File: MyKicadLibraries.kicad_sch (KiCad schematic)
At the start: 38 parts, among them J1 Conn_01x08, J10 RCJ-22, J11 DIN-5, J12 Mini-DIN-6, J13 USB_A, J14 Conn_01x02, J15 Conn_01x02, J2 Conn_01x08, J3 POGO Pins, J4 c8-inlet, J5 FTDI, J6 Micro_SD_Card, J7 Conn_01x04, J8 Conn_02x04_Counter_Clockwise, J9 Conn_01x04, SW1 Schurter Switch, U1 radio-receiver, U10 rdm-6300, U11 magnetic-charger, U12 adafruit-MAX98357, U13 TTL, U14 lxb18, U15 esp32-wemos-d1-mini, U16 TCRT5000, U17 opb607a, U18 max98367, U19 esp-01f, U2 TP4056, U3 LilygoSIMT7000G, U4 esp-01m, U5 relais_module, U6 ESP-01, U7 dcdc, U8 mems-mic, U9 ESP-12E

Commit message: Update tp4056 and fix edge cut issues
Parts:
- removed BT1: Battery_Cell, symbol Device:Battery_Cell
- removed U2: TP4056, TP4056:TP4056, symbol TP4056:TP4056
- added U2: tp4056, tp4056:tp4056, symbol TP4056:tp4056
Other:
- moved on the sheet: J6, U15, U19
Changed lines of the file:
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@@
     (pin "1")
-  )
-  (symbol (lib_id "Device:Battery_Cell") (at 121.92 158.75 0) (unit 1)
-    (in_bom yes) (on_board yes)
-    (property "Reference" "BT1" (id 0) (at 115.824 161.798 90)
-      (effects (font (size 1.27 1.27)) (justify left))
-    )
-    (property "Value" "Battery_Cell" (id 1) (at 118.364 161.798 90)
-      (effects (font (size 1.27 1.27)) (justify left))
-    )
-    (property "Footprint" "" (id 2) (at 121.92 157.226 90)
-      (effects (font (size 1.27 1.27)) hide)
-    )
-    (property "Datasheet" "~" (id 3) (at 121.92 157.226 90)
-      (effects (font (size 1.27 1.27)) hide)
-    )
-    (pin "1")
-    (pin "2")
   )
   (symbol (lib_id "Connector:DIN-5") (at 158.75 97.79 0) (unit 1)
@@
     (pin "9")
   )
-  (symbol (lib_id "esp32-wemos-d1-mini:esp32-wemos-d1-mini") (at -22.098 87.376 0) (unit 1)
-    (in_bom yes) (on_board yes) (fields_autoplaced)
-    (property "Reference" "U15" (id 0) (at -21.463 83.82 0))
-    (property "Value" "esp32-wemos-d1-mini" (id 1) (at -21.463 86.36 0))
-    (property "Footprint" "esp32-wemos-d1-mini:esp32-wemos-d1-mini" (id 2) (at -18.288 84.836 0)
-      (effects (font (size 1.27 1.27)) hide)
-    )
-    (property "Datasheet" "" (id 3) (at -18.288 84.836 0)
+  (symbol (lib_id "esp32-wemos-d1-mini:esp32-wemos-d1-mini") (at 276.86 38.1 0) (unit 1)
+    (in_bom yes) (on_board yes) (fields_autoplaced)
+    (property "Reference" "U15" (id 0) (at 277.495 34.544 0))
+    (property "Value" "esp32-wemos-d1-mini" (id 1) (at 277.495 37.084 0))
+    (property "Footprint" "esp32-wemos-d1-mini:esp32-wemos-d1-mini" (id 2) (at 280.67 35.56 0)
+      (effects (font (size 1.27 1.27)) hide)
+    )
+    (property "Datasheet" "" (id 3) (at 280.67 35.56 0)
       (effects (font (size 1.27 1.27)) hide)
     )
@@
     (pin "8")
   )
-  (symbol (lib_id "TP4056:TP4056") (at 129.54 157.48 0) (unit 1)
-    (in_bom yes) (on_board yes) (fields_autoplaced)
-    (property "Reference" "U2" (id 0) (at 131.5594 146.05 0)
-      (effects (font (size 1.27 1.27)) (justify left))
-    )
-    (property "Value" "TP4056" (id 1) (at 131.5594 148.59 0)
-      (effects (font (size 1.27 1.27)) (justify left))
-    )
-    (property "Footprint" "TP4056:TP4056" (id 2) (at 128.27 131.445 0)
-      (effects (font (size 1.27 1.27)) hide)
-    )
-    (property "Datasheet" "" (id 3) (at 128.27 131.445 0)
-      (effects (font (size 1.27 1.27)) hide)
-    )
-    (pin "1")
-    (pin "2")
-    (pin "3")
-    (pin "4")
-    (pin "5")
-    (pin "6")
-  )
-  (symbol (lib_id "Connector:Micro_SD_Card") (at 83.566 172.466 0) (unit 1)
-    (in_bom yes) (on_board yes) (fields_autoplaced)
-    (property "Reference" "J6" (id 0) (at 84.201 152.654 0))
-    (property "Value" "Micro_SD_Card" (id 1) (at 84.201 155.194 0))
-    (property "Footprint" "sd-card:sd-card" (id 2) (at 112.776 164.846 0)
-      (effects (font (size 1.27 1.27)) hide)
-    )
-    (property "Datasheet" "http://katalog.we-online.de/em/datasheet/693072010801.pdf" (id 3) (at 83.566 172.466 0)
+  (symbol (lib_id "Connector:Micro_SD_Card") (at 39.37 176.53 0) (unit 1)
+    (in_bom yes) (on_board yes) (fields_autoplaced)
+    (property "Reference" "J6" (id 0) (at 40.005 156.718 0))
+    (property "Value" "Micro_SD_Card" (id 1) (at 40.005 159.258 0))
+    (property "Footprint" "sd-card:sd-card" (id 2) (at 68.58 168.91 0)
+      (effects (font (size 1.27 1.27)) hide)
+    )
+    (property "Datasheet" "http://katalog.we-online.de/em/datasheet/693072010801.pdf" (id 3) (at 39.37 176.53 0)
       (effects (font (size 1.27 1.27)) hide)
     )
@@
     (pin "3")
   )
-  (symbol (lib_id "esp-01F:esp-01f") (at -73.787 111.125 0) (unit 1)
-    (in_bom yes) (on_board yes) (fields_autoplaced)
-    (property "Reference" "U19" (id 0) (at -73.787 85.09 0))
-    (property "Value" "esp-01f" (id 1) (at -73.787 87.63 0))
-    (property "Footprint" "esp-01f:esp-01f" (id 2) (at -87.122 142.875 0)
+  (symbol (lib_id "esp-01F:esp-01f") (at 86.36 167.64 0) (unit 1)
+    (in_bom yes) (on_board yes) (fields_autoplaced)
+    (property "Reference" "U19" (id 0) (at 86.36 141.605 0))
+    (property "Value" "esp-01f" (id 1) (at 86.36 144.145 0))
+    (property "Footprint" "esp-01f:esp-01f" (id 2) (at 73.025 199.39 0)
       (effects (font (size 1.27 1.27)) (justify bottom) hide)
     )
-    (property "Datasheet" "http://www.ai-thinker.com/pro_view-62.html" (id 3) (at -72.517 139.7 0)
+    (property "Datasheet" "http://www.ai-thinker.com/pro_view-62.html" (id 3) (at 87.63 196.215 0)
       (effects (font (size 1.27 1.27)) hide)
     )
@@
     (pin "4")
   )
+  (symbol (lib_id "TP4056:tp4056") (at 26.67 73.66 0) (unit 1)
+    (in_bom yes) (on_board yes) (fields_autoplaced)
+    (property "Reference" "U2" (id 0) (at 28.6894 62.23 0)
+      (effects (font (size 1.27 1.27)) (justify left))
+    )
+    (property "Value" "tp4056" (id 1) (at 28.6894 64.77 0)
+      (effects (font (size 1.27 1.27)) (justify left))
+    )
+    (property "Footprint" "tp4056:tp4056" (id 2) (at 25.4 47.625 0)
+      (effects (font (size 1.27 1.27)) hide)
+    )
+    (property "Datasheet" "" (id 3) (at 25.4 47.625 0)
+      (effects (font (size 1.27 1.27)) hide)
+    )
+    (pin "1")
+    (pin "2")
+    (pin "2")
+    (pin "3")
+    (pin "3")
+    (pin "6")
+  )
   (symbol (lib_id "Connector_Generic:Conn_01x04") (at 260.604 29.21 0) (mirror x) (unit 1)
     (in_bom yes) (on_board yes) (fields_autoplaced)
@@
       (reference "#PWR0103") (unit 1) (value "GND") (footprint "")
     )
-    (path "/0cd8403f-406a-4eab-8a59-bcebc0593a4b"
-      (reference "BT1") (unit 1) (value "Battery_Cell") (footprint "")
-    )
     (path "/d968a578-d892-4ece-acfe-f95f8b4cdb95"
       (reference "J1") (unit 1) (value "Conn_01x08") (footprint "Connector_PinHeader_2.54mm:PinHeader_1x08_P2.54mm_Vertical")
@@
       (reference "U1") (unit 1) (value "radio-receiver") (footprint "radio-receiver:radio-receiver")
     )
-    (path "/8e4cc5f0-d50f-4454-b7ee-302278541603"
-      (reference "U2") (unit 1) (value "TP4056") (footprint "TP4056:TP4056")
+    (path "/be776797-d185-4aa8-885c-a32f4e60d5ee"
+      (reference "U2") (unit 1) (value "tp4056") (footprint "tp4056:tp4056")
     )
     (path "/cbd25838-12dc-4905-881f-041585a74948"

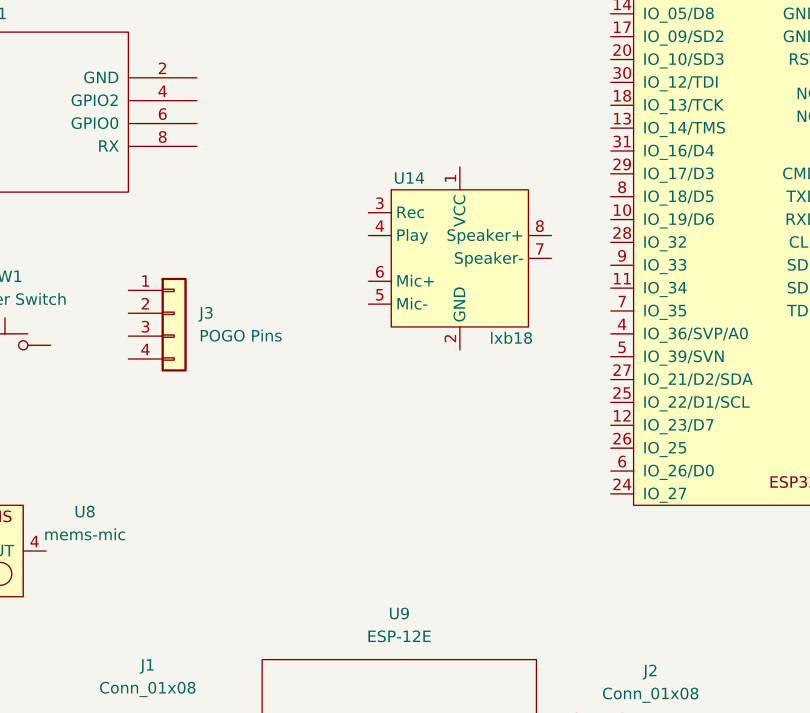
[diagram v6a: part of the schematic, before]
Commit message: Add m18 bluetooth module
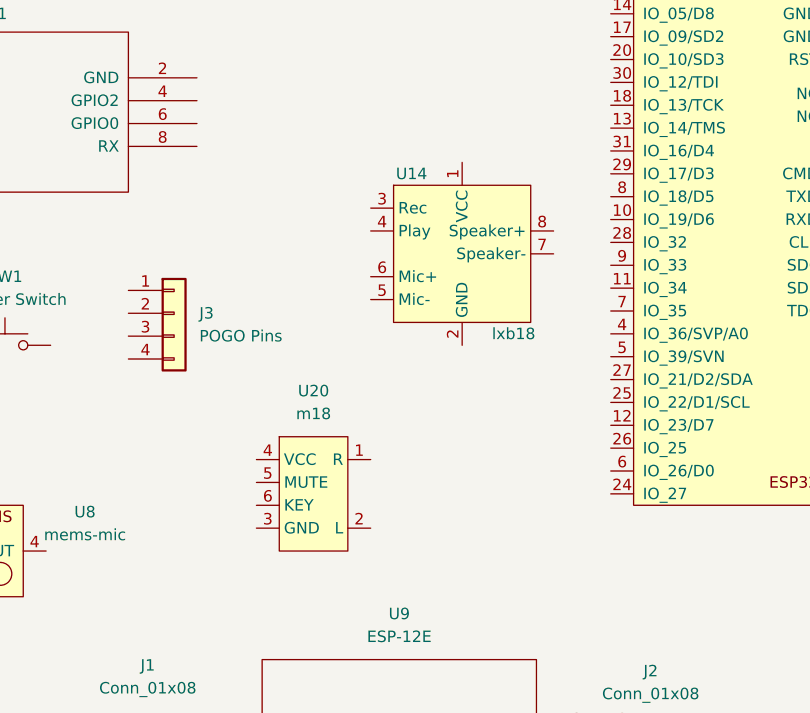
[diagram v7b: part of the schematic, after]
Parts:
- added U20: m18, m18:m18, symbol m18:m18
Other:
- moved on the sheet: U14
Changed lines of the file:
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@@
     (pin "2")
   )
-  (symbol (lib_id "lxb18:lxb18") (at 247.396 75.438 0) (unit 1)
+  (symbol (lib_id "lxb18:lxb18") (at 247.65 74.93 0) (unit 1)
     (in_bom yes) (on_board yes)
-    (property "Reference" "U14" (id 0) (at 240.03 66.548 0)
+    (property "Reference" "U14" (id 0) (at 240.284 66.04 0)
       (effects (font (size 1.27 1.27)) (justify left))
     )
-    (property "Value" "lxb18" (id 1) (at 250.698 84.328 0)
+    (property "Value" "lxb18" (id 1) (at 250.952 83.82 0)
       (effects (font (size 1.27 1.27)) (justify left))
     )
-    (property "Footprint" "lxb18:lxb18" (id 2) (at 242.316 75.438 0)
-      (effects (font (size 1.27 1.27)) hide)
-    )
-    (property "Datasheet" "" (id 3) (at 242.316 75.438 0)
+    (property "Footprint" "lxb18:lxb18" (id 2) (at 242.57 74.93 0)
+      (effects (font (size 1.27 1.27)) hide)
+    )
+    (property "Datasheet" "" (id 3) (at 242.57 74.93 0)
       (effects (font (size 1.27 1.27)) hide)
     )
@@
     (pin "7")
     (pin "8")
+  )
+  (symbol (lib_id "m18:m18") (at 231.14 101.6 0) (unit 1)
+    (in_bom yes) (on_board yes) (fields_autoplaced)
+    (property "Reference" "U20" (id 0) (at 231.14 90.17 0))
+    (property "Value" "m18" (id 1) (at 231.14 92.71 0))
+    (property "Footprint" "m18:m18" (id 2) (at 231.14 119.38 0)
+      (effects (font (size 1.27 1.27)) hide)
+    )
+    (property "Datasheet" "https://www.sunrom.com/download/705.pdf" (id 3) (at 233.68 121.92 0)
+      (effects (font (size 1.27 1.27)) hide)
+    )
+    (pin "1")
+    (pin "2")
+    (pin "3")
+    (pin "4")
+    (pin "5")
+    (pin "6")
   )
   (symbol (lib_id "Connector:Micro_SD_Card") (at 39.37 176.53 0) (unit 1)
@@
       (reference "U19") (unit 1) (value "esp-01f") (footprint "esp-01f:esp-01f")
     )
-  )
+    (path "/8c5c232b-954a-4341-8eca-3f983293a8fb"
+      (reference "U20") (unit 1) (value "m18") (footprint "m18:m18")
+    )
+  )

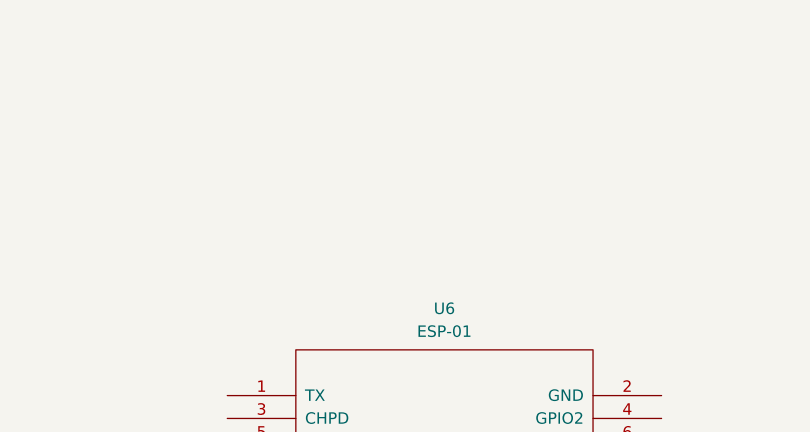
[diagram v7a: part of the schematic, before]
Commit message: Add bme280 submodule
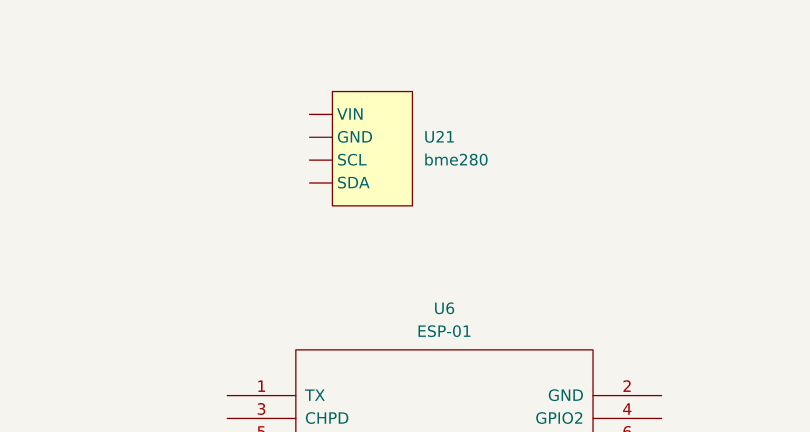
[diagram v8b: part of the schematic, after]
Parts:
- added U21: bme280, bme280:bme280, symbol bme280:bme280
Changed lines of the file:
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@@
     (pin "1")
+  )
+  (symbol (lib_id "bme280:bme280") (at 185.42 27.94 0) (unit 1)
+    (in_bom yes) (on_board yes) (fields_autoplaced)
+    (property "Reference" "U21" (id 0) (at 191.77 26.6699 0)
+      (effects (font (size 1.27 1.27)) (justify left))
+    )
+    (property "Value" "bme280" (id 1) (at 191.77 29.2099 0)
+      (effects (font (size 1.27 1.27)) (justify left))
+    )
+    (property "Footprint" "bme280:bme280" (id 2) (at 185.42 27.94 0)
+      (effects (font (size 1.27 1.27)) hide)
+    )
+    (property "Datasheet" "https://www.mouser.com/datasheet/2/783/BST-BME280-DS002-1509607.pdf" (id 3) (at 185.42 27.94 0)
+      (effects (font (size 1.27 1.27)) hide)
+    )
+    (pin "")
+    (pin "")
+    (pin "")
+    (pin "")
   )
   (symbol (lib_id "power:GND") (at 60.325 83.185 0) (unit 1)
@@
       (reference "U20") (unit 1) (value "m18") (footprint "m18:m18")
     )
-  )
+    (path "/06cd0ca5-5eff-4032-bb89-6a28866f3c0c"
+      (reference "U21") (unit 1) (value "bme280") (footprint "bme280:bme280")
+    )
+  )
